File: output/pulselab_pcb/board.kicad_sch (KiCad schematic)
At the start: 4 parts

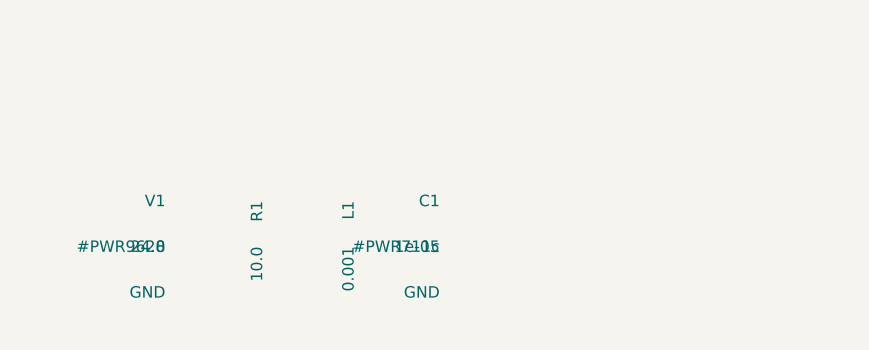
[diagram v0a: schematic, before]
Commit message: feat: implement PCB editor with component placement, multi-selection, and wire routing capabilities
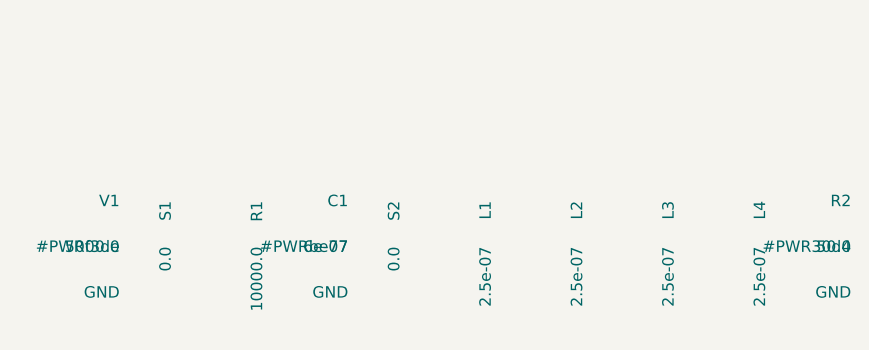
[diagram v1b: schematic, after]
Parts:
- added L2, L3, L4: 2.5e-07, symbol Device:L
- added R2: 50.0, symbol Device:R
- added S1, S2: 0.0, symbol Switch:SW_Push
- C1: value 1e-05 -> 6e-07
- L1: value 0.001 -> 2.5e-07
- R1: value 10.0 -> 10000.0
- V1: value 24.0 -> 5000.0
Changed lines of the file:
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@@
 (kicad_sch (version 20231120) (generator "PulseLab_Forge")
   (paper "A4")
-  (symbol (lib_id "Device:Battery_Cell") (at 60.16 70.32 0) (unit 1)
+  (symbol (lib_id "Device:Battery_Cell") (at 55.08 70.32 0) (unit 1)
     (in_bom yes) (on_board yes) (dnp no) (fields_autoplaced)
-    (property "Reference" "V1" (at 60.16 67.77999999999999 0)
+    (property "Reference" "V1" (at 55.08 67.77999999999999 0)
       (effects (font (size 1.27 1.27)) (justify right))
     )
-    (property "Value" "24.0" (at 60.16 72.86 0)
+    (property "Value" "5000.0" (at 55.08 72.86 0)
+      (effects (font (size 1.27 1.27)) (justify right))
+    )
+  )
+  (symbol (lib_id "Switch:SW_Push") (at 60.16 70.32 90) (unit 1)
+    (in_bom yes) (on_board yes) (dnp no) (fields_autoplaced)
+    (property "Reference" "S1" (at 60.16 67.77999999999999 0)
+      (effects (font (size 1.27 1.27)) (justify right))
+    )
+    (property "Value" "0.0" (at 60.16 72.86 0)
       (effects (font (size 1.27 1.27)) (justify right))
     )
@@
       (effects (font (size 1.27 1.27)) (justify right))
     )
-    (property "Value" "10.0" (at 70.32 72.86 0)
+    (property "Value" "10000.0" (at 70.32 72.86 0)
       (effects (font (size 1.27 1.27)) (justify right))
     )
   )
-  (symbol (lib_id "Device:L") (at 80.48 70.32 90) (unit 1)
+  (symbol (lib_id "Device:C") (at 80.48 70.32 0) (unit 1)
     (in_bom yes) (on_board yes) (dnp no) (fields_autoplaced)
-    (property "Reference" "L1" (at 80.48 67.77999999999999 0)
+    (property "Reference" "C1" (at 80.48 67.77999999999999 0)
       (effects (font (size 1.27 1.27)) (justify right))
     )
-    (property "Value" "0.001" (at 80.48 72.86 0)
+    (property "Value" "6e-07" (at 80.48 72.86 0)
       (effects (font (size 1.27 1.27)) (justify right))
     )
   )
-  (symbol (lib_id "Device:C") (at 90.64 70.32 0) (unit 1)
+  (symbol (lib_id "Switch:SW_Push") (at 85.56 70.32 90) (unit 1)
     (in_bom yes) (on_board yes) (dnp no) (fields_autoplaced)
-    (property "Reference" "C1" (at 90.64 67.77999999999999 0)
+    (property "Reference" "S2" (at 85.56 67.77999999999999 0)
       (effects (font (size 1.27 1.27)) (justify right))
     )
-    (property "Value" "1e-05" (at 90.64 72.86 0)
+    (property "Value" "0.0" (at 85.56 72.86 0)
       (effects (font (size 1.27 1.27)) (justify right))
     )
   )
-  (symbol (lib_id "power:GND") (at 60.16 75.4 0) (unit 1)
+  (symbol (lib_id "Device:L") (at 95.72 70.32 90) (unit 1)
     (in_bom yes) (on_board yes) (dnp no) (fields_autoplaced)
-    (property "Reference" "#PWR9628" (at 60.16 72.86 0)
+    (property "Reference" "L1" (at 95.72 67.77999999999999 0)
       (effects (font (size 1.27 1.27)) (justify right))
     )
-    (property "Value" "GND" (at 60.16 77.94000000000001 0)
+    (property "Value" "2.5e-07" (at 95.72 72.86 0)
       (effects (font (size 1.27 1.27)) (justify right))
     )
   )
-  (symbol (lib_id "power:GND") (at 90.64 75.4 0) (unit 1)
+  (symbol (lib_id "Device:L") (at 105.88 70.32 90) (unit 1)
     (in_bom yes) (on_board yes) (dnp no) (fields_autoplaced)
-    (property "Reference" "#PWR711c" (at 90.64 72.86 0)
+    (property "Reference" "L2" (at 105.88 67.77999999999999 0)
       (effects (font (size 1.27 1.27)) (justify right))
     )
-    (property "Value" "GND" (at 90.64 77.94000000000001 0)
+    (property "Value" "2.5e-07" (at 105.88 72.86 0)
       (effects (font (size 1.27 1.27)) (justify right))
     )
+  )
+  (symbol (lib_id "Device:L") (at 116.04 70.32 90) (unit 1)
+    (in_bom yes) (on_board yes) (dnp no) (fields_autoplaced)
+    (property "Reference" "L3" (at 116.04 67.77999999999999 0)
+      (effects (font (size 1.27 1.27)) (justify right))
+    )
+    (property "Value" "2.5e-07" (at 116.04 72.86 0)
+      (effects (font (size 1.27 1.27)) (justify right))
+    )
+  )
+  (symbol (lib_id "Device:L") (at 126.2 70.32 90) (unit 1)
+    (in_bom yes) (on_board yes) (dnp no) (fields_autoplaced)
+    (property "Reference" "L4" (at 126.2 67.77999999999999 0)
+      (effects (font (size 1.27 1.27)) (justify right))
+    )
+    (property "Value" "2.5e-07" (at 126.2 72.86 0)
+      (effects (font (size 1.27 1.27)) (justify right))
+    )
+  )
+  (symbol (lib_id "Device:R") (at 136.36 70.32 0) (unit 1)
+    (in_bom yes) (on_board yes) (dnp no) (fields_autoplaced)
+    (property "Reference" "R2" (at 136.36 67.77999999999999 0)
+      (effects (font (size 1.27 1.27)) (justify right))
+    )
+    (property "Value" "50.0" (at 136.36 72.86 0)
+      (effects (font (size 1.27 1.27)) (justify right))
+    )
+  )
+  (symbol (lib_id "power:GND") (at 55.08 75.4 0) (unit 1)
+    (in_bom yes) (on_board yes) (dnp no) (fields_autoplaced)
+    (property "Reference" "#PWRf3de" (at 55.08 72.86 0)
+      (effects (font (size 1.27 1.27)) (justify right))
+    )
+    (property "Value" "GND" (at 55.08 77.94000000000001 0)
+      (effects (font (size 1.27 1.27)) (justify right))
+    )
+  )
+  (symbol (lib_id "power:GND") (at 80.48 75.4 0) (unit 1)
+    (in_bom yes) (on_board yes) (dnp no) (fields_autoplaced)
+    (property "Reference" "#PWRbe77" (at 80.48 72.86 0)
+      (effects (font (size 1.27 1.27)) (justify right))
+    )
+    (property "Value" "GND" (at 80.48 77.94000000000001 0)
+      (effects (font (size 1.27 1.27)) (justify right))
+    )
+  )
+  (symbol (lib_id "power:GND") (at 136.36 75.4 0) (unit 1)
+    (in_bom yes) (on_board yes) (dnp no) (fields_autoplaced)
+    (property "Reference" "#PWR30d4" (at 136.36 72.86 0)
+      (effects (font (size 1.27 1.27)) (justify right))
+    )
+    (property "Value" "GND" (at 136.36 77.94000000000001 0)
+      (effects (font (size 1.27 1.27)) (justify right))
+    )

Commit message: feat: integrate GNN layout modeling and reorganize core circuit engine into project structure
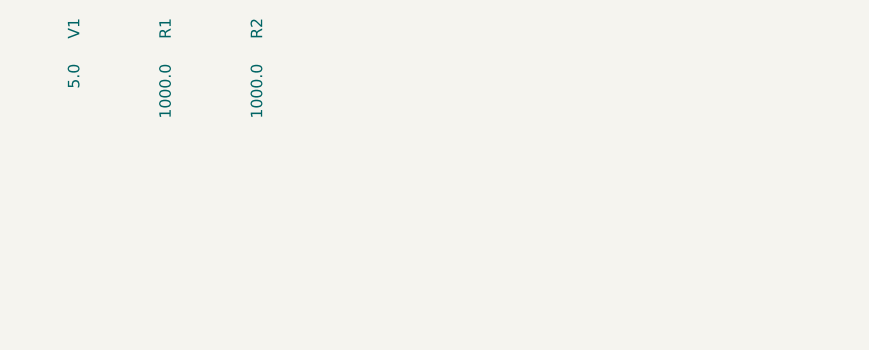
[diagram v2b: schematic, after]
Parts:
- removed C1: 6e-07, symbol Device:C
- removed L1, L2, L3, L4: 2.5e-07, symbol Device:L
- removed S1, S2: 0.0, symbol Switch:SW_Push
- R1: value 10000.0 -> 1000.0
- R2: value 50.0 -> 1000.0
- V1: value 5000.0 -> 5.0
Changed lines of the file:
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@@
 (kicad_sch (version 20231120) (generator "PulseLab_Forge")
   (paper "A4")
-  (symbol (lib_id "Device:Battery_Cell") (at 55.08 70.32 0) (unit 1)
+  (symbol (lib_id "Device:Battery_Cell") (at 50.0 50.0 90) (unit 1)
     (in_bom yes) (on_board yes) (dnp no) (fields_autoplaced)
-    (property "Reference" "V1" (at 55.08 67.77999999999999 0)
+    (property "Reference" "V1" (at 50.0 47.46 0)
       (effects (font (size 1.27 1.27)) (justify right))
     )
-    (property "Value" "5000.0" (at 55.08 72.86 0)
+    (property "Value" "5.0" (at 50.0 52.54 0)
       (effects (font (size 1.27 1.27)) (justify right))
     )
   )
-  (symbol (lib_id "Switch:SW_Push") (at 60.16 70.32 90) (unit 1)
+  (symbol (lib_id "Device:R") (at 60.16 50.0 90) (unit 1)
     (in_bom yes) (on_board yes) (dnp no) (fields_autoplaced)
-    (property "Reference" "S1" (at 60.16 67.77999999999999 0)
+    (property "Reference" "R1" (at 60.16 47.46 0)
       (effects (font (size 1.27 1.27)) (justify right))
     )
-    (property "Value" "0.0" (at 60.16 72.86 0)
+    (property "Value" "1000.0" (at 60.16 52.54 0)
       (effects (font (size 1.27 1.27)) (justify right))
     )
   )
-  (symbol (lib_id "Device:R") (at 70.32 70.32 90) (unit 1)
+  (symbol (lib_id "Device:R") (at 70.32 50.0 90) (unit 1)
     (in_bom yes) (on_board yes) (dnp no) (fields_autoplaced)
-    (property "Reference" "R1" (at 70.32 67.77999999999999 0)
+    (property "Reference" "R2" (at 70.32 47.46 0)
       (effects (font (size 1.27 1.27)) (justify right))
     )
-    (property "Value" "10000.0" (at 70.32 72.86 0)
+    (property "Value" "1000.0" (at 70.32 52.54 0)
       (effects (font (size 1.27 1.27)) (justify right))
     )
-  )
-  (symbol (lib_id "Device:C") (at 80.48 70.32 0) (unit 1)
-    (in_bom yes) (on_board yes) (dnp no) (fields_autoplaced)
-    (property "Reference" "C1" (at 80.48 67.77999999999999 0)
-      (effects (font (size 1.27 1.27)) (justify right))
-    )
-    (property "Value" "6e-07" (at 80.48 72.86 0)
-      (effects (font (size 1.27 1.27)) (justify right))
-    )
-  )
-  (symbol (lib_id "Switch:SW_Push") (at 85.56 70.32 90) (unit 1)
-    (in_bom yes) (on_board yes) (dnp no) (fields_autoplaced)
-    (property "Reference" "S2" (at 85.56 67.77999999999999 0)
-      (effects (font (size 1.27 1.27)) (justify right))
-    )
-    (property "Value" "0.0" (at 85.56 72.86 0)
-      (effects (font (size 1.27 1.27)) (justify right))
-    )
-  )
-  (symbol (lib_id "Device:L") (at 95.72 70.32 90) (unit 1)
-    (in_bom yes) (on_board yes) (dnp no) (fields_autoplaced)
-    (property "Reference" "L1" (at 95.72 67.77999999999999 0)
-      (effects (font (size 1.27 1.27)) (justify right))
-    )
-    (property "Value" "2.5e-07" (at 95.72 72.86 0)
-      (effects (font (size 1.27 1.27)) (justify right))
-    )
-  )
-  (symbol (lib_id "Device:L") (at 105.88 70.32 90) (unit 1)
-    (in_bom yes) (on_board yes) (dnp no) (fields_autoplaced)
-    (property "Reference" "L2" (at 105.88 67.77999999999999 0)
-      (effects (font (size 1.27 1.27)) (justify right))
-    )
-    (property "Value" "2.5e-07" (at 105.88 72.86 0)
-      (effects (font (size 1.27 1.27)) (justify right))
-    )
-  )
-  (symbol (lib_id "Device:L") (at 116.04 70.32 90) (unit 1)
-    (in_bom yes) (on_board yes) (dnp no) (fields_autoplaced)
-    (property "Reference" "L3" (at 116.04 67.77999999999999 0)
-      (effects (font (size 1.27 1.27)) (justify right))
-    )
-    (property "Value" "2.5e-07" (at 116.04 72.86 0)
-      (effects (font (size 1.27 1.27)) (justify right))
-    )
-  )
-  (symbol (lib_id "Device:L") (at 126.2 70.32 90) (unit 1)
-    (in_bom yes) (on_board yes) (dnp no) (fields_autoplaced)
-    (property "Reference" "L4" (at 126.2 67.77999999999999 0)
-      (effects (font (size 1.27 1.27)) (justify right))
-    )
-    (property "Value" "2.5e-07" (at 126.2 72.86 0)
-      (effects (font (size 1.27 1.27)) (justify right))
-    )
-  )
-  (symbol (lib_id "Device:R") (at 136.36 70.32 0) (unit 1)
-    (in_bom yes) (on_board yes) (dnp no) (fields_autoplaced)
-    (property "Reference" "R2" (at 136.36 67.77999999999999 0)
-      (effects (font (size 1.27 1.27)) (justify right))
-    )
-    (property "Value" "50.0" (at 136.36 72.86 0)
-      (effects (font (size 1.27 1.27)) (justify right))
-    )
-  )
-  (symbol (lib_id "power:GND") (at 55.08 75.4 0) (unit 1)
-    (in_bom yes) (on_board yes) (dnp no) (fields_autoplaced)
-    (property "Reference" "#PWRf3de" (at 55.08 72.86 0)
-      (effects (font (size 1.27 1.27)) (justify right))
-    )
-    (property "Value" "GND" (at 55.08 77.94000000000001 0)
-      (effects (font (size 1.27 1.27)) (justify right))
-    )
-  )
-  (symbol (lib_id "power:GND") (at 80.48 75.4 0) (unit 1)
-    (in_bom yes) (on_board yes) (dnp no) (fields_autoplaced)
-    (property "Reference" "#PWRbe77" (at 80.48 72.86 0)
-      (effects (font (size 1.27 1.27)) (justify right))
-    )
-    (property "Value" "GND" (at 80.48 77.94000000000001 0)
-      (effects (font (size 1.27 1.27)) (justify right))
-    )
-  )
-  (symbol (lib_id "power:GND") (at 136.36 75.4 0) (unit 1)
-    (in_bom yes) (on_board yes) (dnp no) (fields_autoplaced)
-    (property "Reference" "#PWR30d4" (at 136.36 72.86 0)
-      (effects (font (size 1.27 1.27)) (justify right))
-    )
-    (property "Value" "GND" (at 136.36 77.94000000000001 0)
-      (effects (font (size 1.27 1.27)) (justify right))
-    )

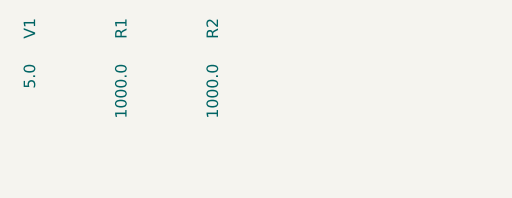
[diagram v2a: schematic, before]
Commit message: data: ingest raw kicad files and training samples
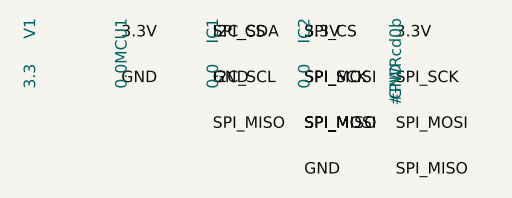
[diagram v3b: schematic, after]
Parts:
- removed R1, R2: 1000.0, symbol Device:R
- added IC1, IC2, MCU1: 0.0, symbol MCU_Espressif:ESP8266EX
- V1: value 5.0 -> 3.3
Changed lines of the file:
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@@
       (effects (font (size 1.27 1.27)) (justify right))
     )
-    (property "Value" "5.0" (at 50.0 52.54 0)
+    (property "Value" "3.3" (at 50.0 52.54 0)
       (effects (font (size 1.27 1.27)) (justify right))
     )
   )
-  (symbol (lib_id "Device:R") (at 60.16 50.0 90) (unit 1)
+  (label "3.3V" (at 60.16 50.0 0) (fields_autoplaced)
+    (effects (font (size 1.27 1.27)) (justify left bottom))
+  )
+  (label "GND" (at 60.16 55.08 0) (fields_autoplaced)
+    (effects (font (size 1.27 1.27)) (justify left bottom))
+  )
+  (label "I2C_SCL" (at 70.32 55.08 0) (fields_autoplaced)
+    (effects (font (size 1.27 1.27)) (justify left bottom))
+  )
+  (label "I2C_SDA" (at 70.32 50.0 0) (fields_autoplaced)
+    (effects (font (size 1.27 1.27)) (justify left bottom))
+  )
+  (symbol (lib_id "MCU_Espressif:ESP8266EX") (at 60.16 50.0 90) (unit 1)
     (in_bom yes) (on_board yes) (dnp no) (fields_autoplaced)
-    (property "Reference" "R1" (at 60.16 47.46 0)
+    (property "Reference" "MCU1" (at 60.16 47.46 0)
       (effects (font (size 1.27 1.27)) (justify right))
     )
-    (property "Value" "1000.0" (at 60.16 52.54 0)
+    (property "Value" "0.0" (at 60.16 52.54 0)
       (effects (font (size 1.27 1.27)) (justify right))
     )
   )
-  (symbol (lib_id "Device:R") (at 70.32 50.0 90) (unit 1)
+  (label "SPI_CS" (at 70.32 50.0 0) (fields_autoplaced)
+    (effects (font (size 1.27 1.27)) (justify left bottom))
+  )
+  (label "GND" (at 70.32 55.08 0) (fields_autoplaced)
+    (effects (font (size 1.27 1.27)) (justify left bottom))
+  )
+  (label "SPI_MISO" (at 70.32 60.16 0) (fields_autoplaced)
+    (effects (font (size 1.27 1.27)) (justify left bottom))
+  )
+  (label "SPI_MOSI" (at 80.48 60.16 0) (fields_autoplaced)
+    (effects (font (size 1.27 1.27)) (justify left bottom))
+  )
+  (label "SPI_SCK" (at 80.48 55.08 0) (fields_autoplaced)
+    (effects (font (size 1.27 1.27)) (justify left bottom))
+  )
+  (label "3.3V" (at 80.48 50.0 0) (fields_autoplaced)
+    (effects (font (size 1.27 1.27)) (justify left bottom))
+  )
+  (symbol (lib_id "MCU_Espressif:ESP8266EX") (at 70.32 50.0 90) (unit 1)
     (in_bom yes) (on_board yes) (dnp no) (fields_autoplaced)
-    (property "Reference" "R2" (at 70.32 47.46 0)
+    (property "Reference" "IC1" (at 70.32 47.46 0)
       (effects (font (size 1.27 1.27)) (justify right))
     )
-    (property "Value" "1000.0" (at 70.32 52.54 0)
+    (property "Value" "0.0" (at 70.32 52.54 0)
       (effects (font (size 1.27 1.27)) (justify right))
     )
+  )
+  (label "SPI_CS" (at 80.48 50.0 0) (fields_autoplaced)
+    (effects (font (size 1.27 1.27)) (justify left bottom))
+  )
+  (label "SPI_MOSI" (at 80.48 55.08 0) (fields_autoplaced)
+    (effects (font (size 1.27 1.27)) (justify left bottom))
+  )
+  (label "SPI_MISO" (at 80.48 60.16 0) (fields_autoplaced)
+    (effects (font (size 1.27 1.27)) (justify left bottom))
+  )
+  (label "GND" (at 80.48 65.24 0) (fields_autoplaced)
+    (effects (font (size 1.27 1.27)) (justify left bottom))
+  )
+  (label "SPI_MISO" (at 90.64 65.24 0) (fields_autoplaced)
+    (effects (font (size 1.27 1.27)) (justify left bottom))
+  )
+  (label "SPI_MOSI" (at 90.64 60.16 0) (fields_autoplaced)
+    (effects (font (size 1.27 1.27)) (justify left bottom))
+  )
+  (label "SPI_SCK" (at 90.64 55.08 0) (fields_autoplaced)
+    (effects (font (size 1.27 1.27)) (justify left bottom))
+  )
+  (label "3.3V" (at 90.64 50.0 0) (fields_autoplaced)
+    (effects (font (size 1.27 1.27)) (justify left bottom))
+  )
+  (symbol (lib_id "MCU_Espressif:ESP8266EX") (at 80.48 50.0 90) (unit 1)
+    (in_bom yes) (on_board yes) (dnp no) (fields_autoplaced)
+    (property "Reference" "IC2" (at 80.48 47.46 0)
+      (effects (font (size 1.27 1.27)) (justify right))
+    )
+    (property "Value" "0.0" (at 80.48 52.54 0)
+      (effects (font (size 1.27 1.27)) (justify right))
+    )
+  )
+  (symbol (lib_id "power:GND") (at 90.64 50.0 90) (unit 1)
+    (in_bom yes) (on_board yes) (dnp no) (fields_autoplaced)
+    (property "Reference" "#PWRcd0b" (at 90.64 47.46 0)
+      (effects (font (size 1.27 1.27)) (justify right))
+    )
+    (property "Value" "GND" (at 90.64 52.54 0)
+      (effects (font (size 1.27 1.27)) (justify right))
+    )

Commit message: feat: initialize knowledge training pipeline with KiCad dataset and supporting utility scripts
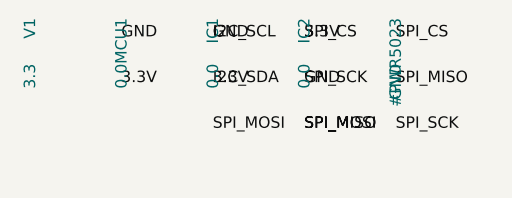
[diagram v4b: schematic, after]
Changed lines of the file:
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@@
     )
   )
-  (label "3.3V" (at 60.16 50.0 0) (fields_autoplaced)
+  (label "GND" (at 60.16 50.0 0) (fields_autoplaced)
     (effects (font (size 1.27 1.27)) (justify left bottom))
   )
-  (label "GND" (at 60.16 55.08 0) (fields_autoplaced)
+  (label "3.3V" (at 60.16 55.08 0) (fields_autoplaced)
     (effects (font (size 1.27 1.27)) (justify left bottom))
   )
-  (label "I2C_SCL" (at 70.32 55.08 0) (fields_autoplaced)
+  (label "I2C_SDA" (at 70.32 55.08 0) (fields_autoplaced)
     (effects (font (size 1.27 1.27)) (justify left bottom))
   )
-  (label "I2C_SDA" (at 70.32 50.0 0) (fields_autoplaced)
+  (label "I2C_SCL" (at 70.32 50.0 0) (fields_autoplaced)
     (effects (font (size 1.27 1.27)) (justify left bottom))
   )
@@
     )
   )
-  (label "SPI_CS" (at 70.32 50.0 0) (fields_autoplaced)
+  (label "GND" (at 70.32 50.0 0) (fields_autoplaced)
     (effects (font (size 1.27 1.27)) (justify left bottom))
   )
-  (label "GND" (at 70.32 55.08 0) (fields_autoplaced)
+  (label "3.3V" (at 70.32 55.08 0) (fields_autoplaced)
     (effects (font (size 1.27 1.27)) (justify left bottom))
   )
-  (label "SPI_MISO" (at 70.32 60.16 0) (fields_autoplaced)
+  (label "SPI_MOSI" (at 70.32 60.16 0) (fields_autoplaced)
     (effects (font (size 1.27 1.27)) (justify left bottom))
   )
-  (label "SPI_MOSI" (at 80.48 60.16 0) (fields_autoplaced)
+  (label "SPI_MISO" (at 80.48 60.16 0) (fields_autoplaced)
     (effects (font (size 1.27 1.27)) (justify left bottom))
   )
@@
     (effects (font (size 1.27 1.27)) (justify left bottom))
   )
-  (label "3.3V" (at 80.48 50.0 0) (fields_autoplaced)
+  (label "SPI_CS" (at 80.48 50.0 0) (fields_autoplaced)
     (effects (font (size 1.27 1.27)) (justify left bottom))
   )
@@
     )
   )
-  (label "SPI_CS" (at 80.48 50.0 0) (fields_autoplaced)
+  (label "3.3V" (at 80.48 50.0 0) (fields_autoplaced)
     (effects (font (size 1.27 1.27)) (justify left bottom))
   )
-  (label "SPI_MOSI" (at 80.48 55.08 0) (fields_autoplaced)
+  (label "GND" (at 80.48 55.08 0) (fields_autoplaced)
     (effects (font (size 1.27 1.27)) (justify left bottom))
   )
-  (label "SPI_MISO" (at 80.48 60.16 0) (fields_autoplaced)
+  (label "SPI_MOSI" (at 80.48 60.16 0) (fields_autoplaced)
     (effects (font (size 1.27 1.27)) (justify left bottom))
   )
-  (label "GND" (at 80.48 65.24 0) (fields_autoplaced)
+  (label "SPI_SCK" (at 90.64 60.16 0) (fields_autoplaced)
     (effects (font (size 1.27 1.27)) (justify left bottom))
   )
-  (label "SPI_MISO" (at 90.64 65.24 0) (fields_autoplaced)
+  (label "SPI_MISO" (at 90.64 55.08 0) (fields_autoplaced)
     (effects (font (size 1.27 1.27)) (justify left bottom))
   )
-  (label "SPI_MOSI" (at 90.64 60.16 0) (fields_autoplaced)
-    (effects (font (size 1.27 1.27)) (justify left bottom))
-  )
-  (label "SPI_SCK" (at 90.64 55.08 0) (fields_autoplaced)
-    (effects (font (size 1.27 1.27)) (justify left bottom))
-  )
-  (label "3.3V" (at 90.64 50.0 0) (fields_autoplaced)
+  (label "SPI_CS" (at 90.64 50.0 0) (fields_autoplaced)
     (effects (font (size 1.27 1.27)) (justify left bottom))
   )
@@
   (symbol (lib_id "power:GND") (at 90.64 50.0 90) (unit 1)
     (in_bom yes) (on_board yes) (dnp no) (fields_autoplaced)
-    (property "Reference" "#PWRcd0b" (at 90.64 47.46 0)
+    (property "Reference" "#PWR5023" (at 90.64 47.46 0)
       (effects (font (size 1.27 1.27)) (justify right))
     )
